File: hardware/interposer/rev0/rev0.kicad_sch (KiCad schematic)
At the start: 14 parts, among them J1 Z80_PLUG_TO_MB, J2 Z80_SOCKET_CPU, J3 5V_INPUT, U1 74AHCT165, U2 74AHCT165, U3 74AHCT165, U4 74AHCT165, U5 PICO_2_W

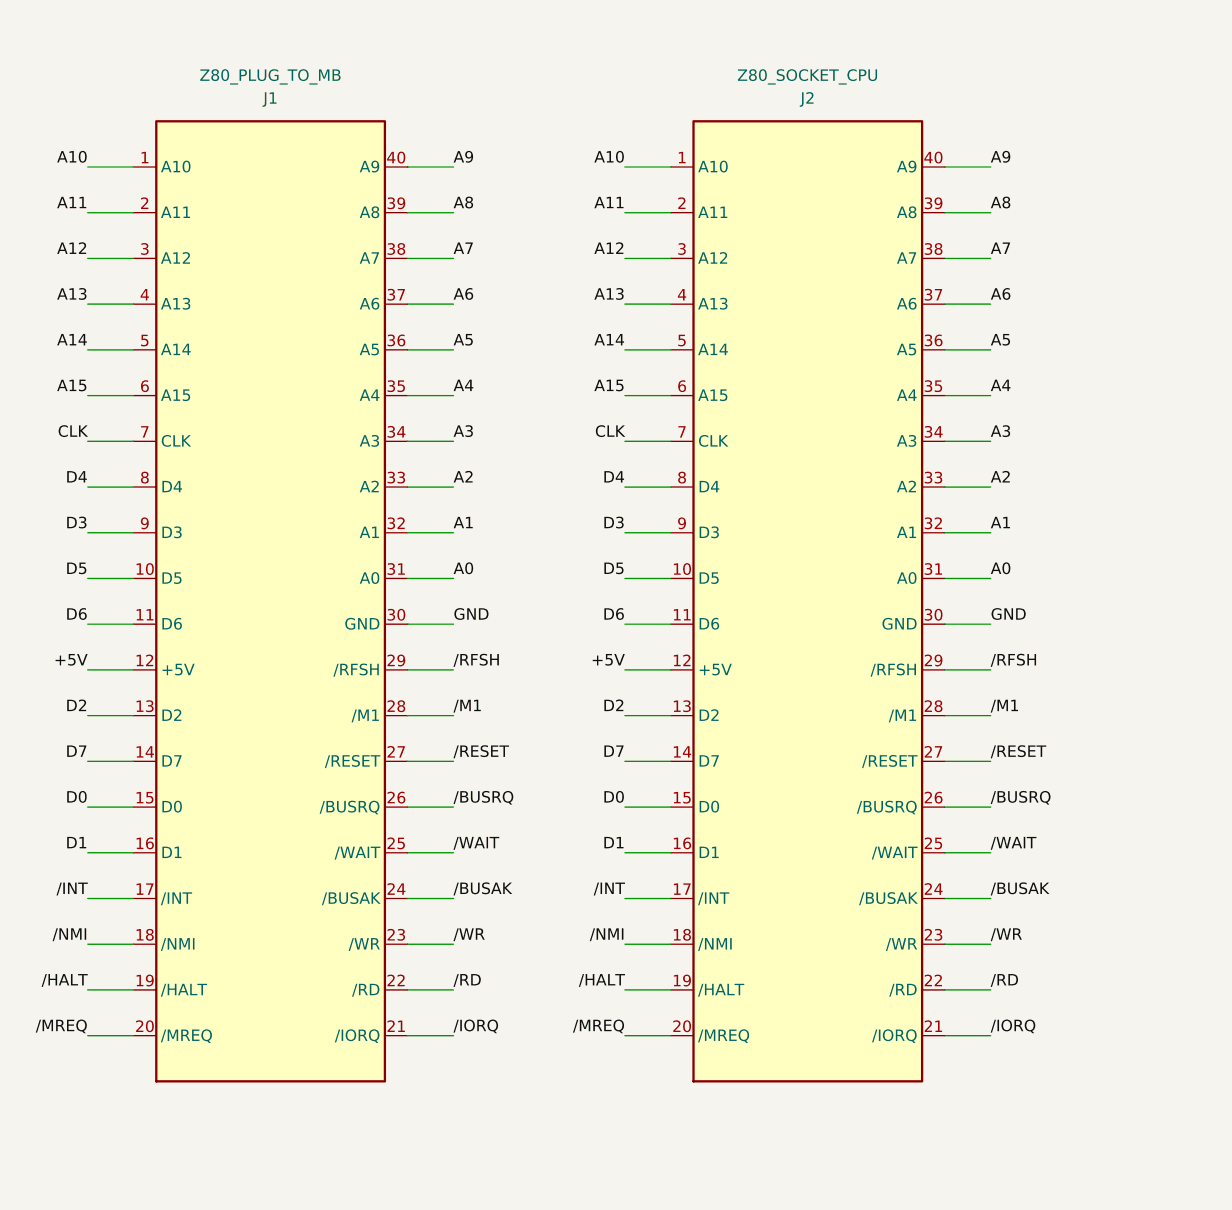
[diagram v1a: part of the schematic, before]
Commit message: hardware: correct the Z80 DIP-40 pinout in the interposer generators (#62)
Both generators carried a Z80 pin table shifted by one pin: pin 1 = A10,
pin 11 = D6, pin 12 = +5V, pin 30 = GND, pin 31 = A0.  The real Zilog DIP-40 is
pin 1 = A11, pin 11 = +5V, pin 29 = GND, pin 30 = A0 (Z80 Microprocessor Family
Databook, cross-checked against z80.info/zinout.htm).  Because J1 plugs into the
O1's Z80 socket and J2/U1 mate with the CPU, every address, data and control
line was tapped one pin off -- the netlist put +5V on the D2 net and shorted
A0 to GND, which would have damaged a real board.

- reva/rev0: define the pinout once (Z80_LEFT/Z80_RIGHT) and derive both the
  symbol geometry and Z80NET from it, reva's Z84C00 symbol included.  Keeping
  two hand-written copies is how the off-by-one survived.
- reva/rev0: 'NC' was used as a net *label*, which ties every unused pin onto
  one net -- on reva that joined four unused 74AHCT595 totem-pole outputs
  (output contention) plus the Z84C00's four NC pins.  Unused pins now get real
  no-connect flags.
- docs/o1-memory-io-map.md sec.6: the Z80 table there was wrong too (it claimed
  pin 11 = GND).  Replaced with the datasheet pinout.
- docs/research-gaps.md gap #3: Z80 half resolved; the char-gen socket pinout
  is still open for the ScreenPac personality (#24).

Reva ERC stays at 12 errors (all genuinely unused pins).  The netlist now reads
correctly: GND = 40 nodes, A0 = J1.30/U1.30/U3.15/U6.11.

part of #62
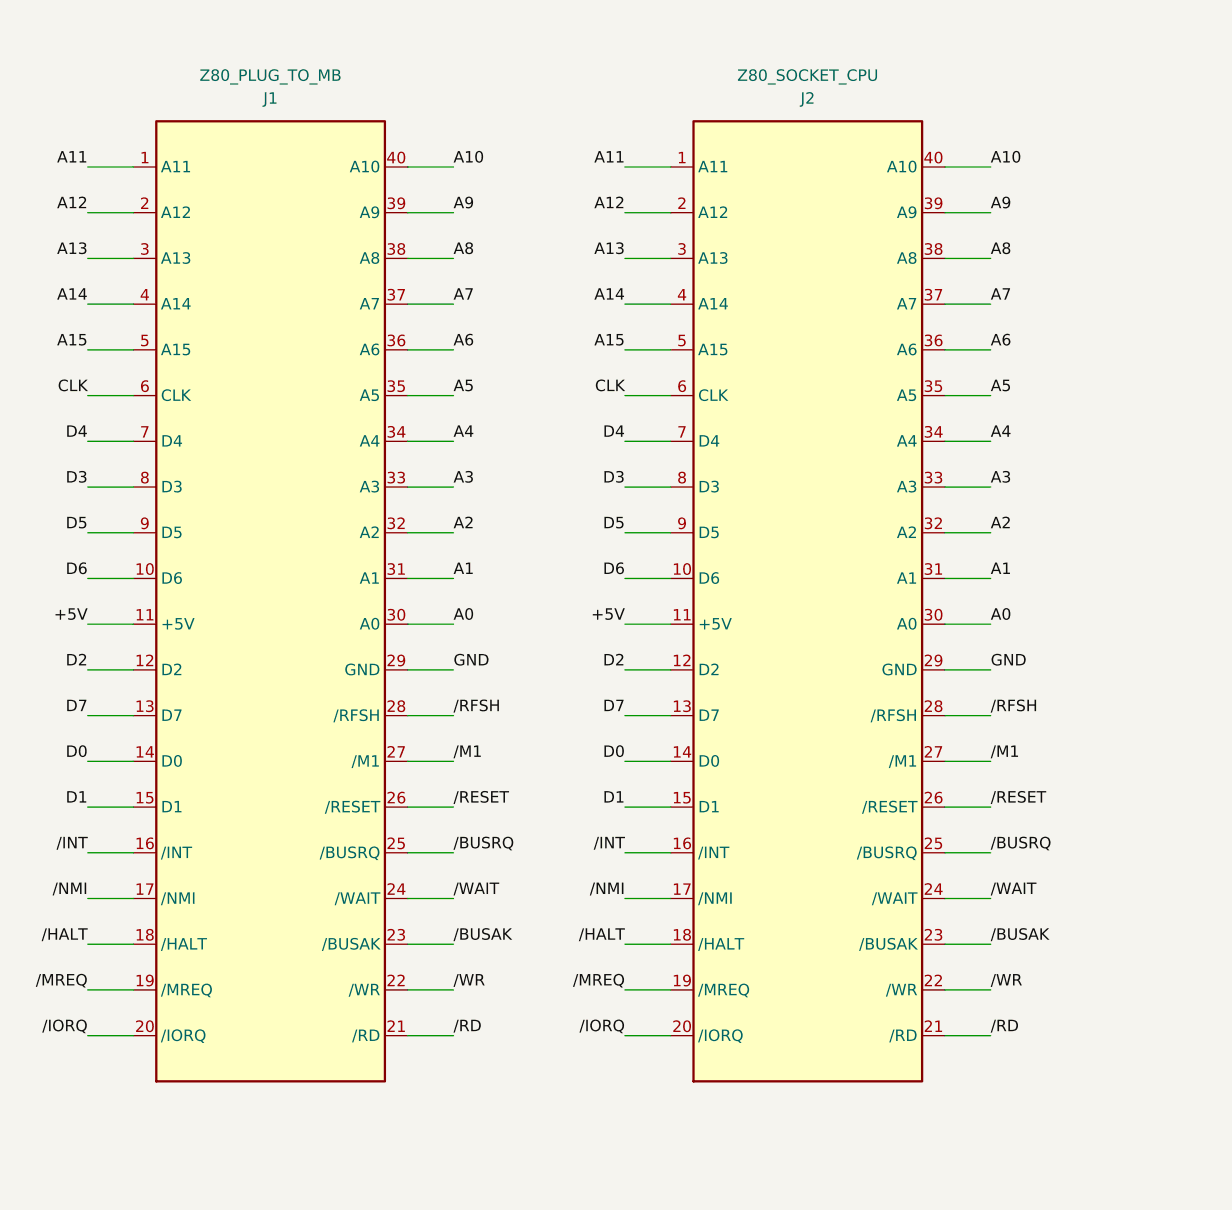
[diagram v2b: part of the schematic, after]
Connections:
- net +5V: now also J1.11 (+5V), J2.11 (+5V); no longer J1.12 (+5V), J2.12 (+5V)
- net /BUSAK: now also J1.23 (/BUSAK), J2.23 (/BUSAK); no longer J1.24 (/BUSAK), J2.24 (/BUSAK)
- net /BUSRQ: now also J1.25 (/BUSRQ), J2.25 (/BUSRQ); no longer J1.26 (/BUSRQ), J2.26 (/BUSRQ)
- net /HALT: now also J1.18 (/HALT), J2.18 (/HALT); no longer J1.19 (/HALT), J2.19 (/HALT)
- net /INT: now also J1.16 (/INT), J2.16 (/INT); no longer J1.17 (/INT), J2.17 (/INT)
- net /IORQ: now also J1.20 (/IORQ), J2.20 (/IORQ); no longer J1.21 (/IORQ), J2.21 (/IORQ)
- net /M1: now also J1.27 (/M1), J2.27 (/M1); no longer J1.28 (/M1), J2.28 (/M1)
- net /MREQ: now also J1.19 (/MREQ), J2.19 (/MREQ); no longer J1.20 (/MREQ), J2.20 (/MREQ)
- net /NMI: now also J1.17 (/NMI), J2.17 (/NMI); no longer J1.18 (/NMI), J2.18 (/NMI)
- net /RD: now also J1.21 (/RD), J2.21 (/RD); no longer J1.22 (/RD), J2.22 (/RD)
- net /RESET: now also J1.26 (/RESET), J2.26 (/RESET); no longer J1.27 (/RESET), J2.27 (/RESET)
- net /RFSH: now also J1.28 (/RFSH), J2.28 (/RFSH); no longer J1.29 (/RFSH), J2.29 (/RFSH)
- net /WAIT: now also J1.24 (/WAIT), J2.24 (/WAIT); no longer J1.25 (/WAIT), J2.25 (/WAIT)
- net /WR: now also J1.22 (/WR), J2.22 (/WR); no longer J1.23 (/WR), J2.23 (/WR)
- net A0: now also J1.30 (A0), J2.30 (A0); no longer J1.31 (A0), J2.31 (A0)
- net A1: now also J1.31 (A1), J2.31 (A1); no longer J1.32 (A1), J2.32 (A1)
- net A10: now also J1.40 (A10), J2.40 (A10); no longer J1.1 (A10), J2.1 (A10)
- net A11: now also J1.1 (A11), J2.1 (A11); no longer J1.2 (A11), J2.2 (A11)
- net A12: now also J1.2 (A12), J2.2 (A12); no longer J1.3 (A12), J2.3 (A12)
- net A13: now also J1.3 (A13), J2.3 (A13); no longer J1.4 (A13), J2.4 (A13)
- net A14: now also J1.4 (A14), J2.4 (A14); no longer J1.5 (A14), J2.5 (A14)
- net A15: now also J1.5 (A15), J2.5 (A15); no longer J1.6 (A15), J2.6 (A15)
- net A2: now also J1.32 (A2), J2.32 (A2); no longer J1.33 (A2), J2.33 (A2)
- net A3: now also J1.33 (A3), J2.33 (A3); no longer J1.34 (A3), J2.34 (A3)
- net A4: now also J1.34 (A4), J2.34 (A4); no longer J1.35 (A4), J2.35 (A4)
- net A5: now also J1.35 (A5), J2.35 (A5); no longer J1.36 (A5), J2.36 (A5)
- net A6: now also J1.36 (A6), J2.36 (A6); no longer J1.37 (A6), J2.37 (A6)
- net A7: now also J1.37 (A7), J2.37 (A7); no longer J1.38 (A7), J2.38 (A7)
- net A8: now also J1.38 (A8), J2.38 (A8); no longer J1.39 (A8), J2.39 (A8)
- net A9: now also J1.39 (A9), J2.39 (A9); no longer J1.40 (A9), J2.40 (A9)
- net CLK: now also J1.6 (CLK), J2.6 (CLK); no longer J1.7 (CLK), J2.7 (CLK)
- net D0: now also J1.14 (D0), J2.14 (D0); no longer J1.15 (D0), J2.15 (D0)
- net D1: now also J1.15 (D1), J2.15 (D1); no longer J1.16 (D1), J2.16 (D1)
- net D2: now also J1.12 (D2), J2.12 (D2); no longer J1.13 (D2), J2.13 (D2)
- net D3: now also J1.8 (D3), J2.8 (D3); no longer J1.9 (D3), J2.9 (D3)
- net D4: now also J1.7 (D4), J2.7 (D4); no longer J1.8 (D4), J2.8 (D4)
- net D5: now also J1.9 (D5), J2.9 (D5); no longer J1.10 (D5), J2.10 (D5)
- net D6: now also J1.10 (D6), J2.10 (D6); no longer J1.11 (D6), J2.11 (D6)
- net D7: now also J1.13 (D7), J2.13 (D7); no longer J1.14 (D7), J2.14 (D7)
- net GND: now also J1.29 (GND), J2.29 (GND); no longer J1.30 (GND), J2.30 (GND)
